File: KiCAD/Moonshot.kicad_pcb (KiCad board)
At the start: 2 copper layers, 33.7 x 40 mm, 16 parts, among them J1 USB-AF-DIP-154-HW-S_P1, J2 USB-AF-DIP-154-HW-S_P2, J3 DE9_Plug, J6 no impl., SW1 SW_Push, U1 CH559L, U2 74LS257, U3 74LS257

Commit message: v3 pcb
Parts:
- added J4: HY2.0-4P, toyoshim:CONN-TH_4P-P2.00_HX20020-4A_2, F.Cu at (40.4, 48.6)
- moved J6 18.2 mm to (22.9, 49.5)
- moved U2 17.0 mm to (46.4, 40.1), turned to 90 degrees
- moved C5 12.5 mm to (43.6, 35.9), turned to 180 degrees
- moved C6 8.78 mm to (25.1, 35.9), turned to 180 degrees
- moved U1 7.01 mm to (36.2, 40.0), turned to -90 degrees
- moved C2 6.79 mm to (41.8, 39.6), turned to 90 degrees
- moved C1 4.58 mm to (41.8, 41.5), turned to -90 degrees
- moved U3 3.24 mm to (27.9, 40.1), turned to 90 degrees
- moved C4 2.67 mm to (34.3, 51.4)
- moved C3 2.21 mm to (18.4, 51.4)
- moved R1 0.90 mm to (47.6, 49.5)
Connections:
- U1 pad 38: unconnected-(U1-P0_2-Pad38) -> /SDA
- U1 pad 39: unconnected-(U1-P0_1-Pad39) -> /SCL
- U1 pad 43: unconnected-(U1-P1_0-Pad43) -> /SDA
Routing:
- net /SCL: track 0.00 -> 70.5 mm, vias 0 -> 2
- net /B5: track 61.9 -> 15.4 mm
- net /B2: track 47.9 -> 6.81 mm, vias 2 -> 0
- net /JOY_B2: track 15.7 -> 56.6 mm, vias 1 -> 0
- net /START: track 51.9 -> 13.5 mm, vias 2 -> 0
- net /B6: track 54.1 -> 15.8 mm, vias 2 -> 0
- net VCC: track 84.6 -> 120.9 mm, vias 1 -> 2
- net /BTN: track 52.2 -> 17.9 mm, vias 2 -> 0
- net /B4: track 34.1 -> 8.01 mm
- net /B1: track 28.7 -> 52.1 mm
- net /SDA: track 0.00 -> 21.8 mm
- net /UP: track 13.4 -> 35.1 mm
- net GND: track 153.1 -> 170.6 mm, vias 1 -> 2
- net /TXD: track 4.97 -> 22.3 mm, vias 0 -> 2
- net /JOY_U: track 17.7 -> 34.7 mm
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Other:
- board text added: "2023.11.25 Rev.3 Designed By Mellow PCB MP17-MOONSHOT"
- board text added: "GND VCC SDA SCL"
- board text added: "I"
- board text added: "□"
- board text removed: "2023.10.22 Rev.2 Designed By Mellow PCB MP17-MOONSHOT"

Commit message: Moonshot rev.4 board
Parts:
- moved C5 0.76 mm to (42.8, 35.9)
- moved U2 0.76 mm to (45.6, 40.1)
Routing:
- net GND: track 170.6 -> 98.1 mm, vias 2 -> 8
- net /SCL: track 70.5 -> 10.8 mm, vias 2 -> 1
- net /JOY_B2: track 56.6 -> 13.6 mm, vias 0 -> 1
- net /B1: track 52.1 -> 18.8 mm
- net /JOY_R: track 10.5 -> 35.8 mm, vias 0 -> 1
- net VCC: track 120.9 -> 96.2 mm, vias 2 -> 3
- net /JOY_COM: track 85.4 -> 66.7 mm, vias 3 -> 2
- net /TXD: track 22.3 -> 36.6 mm, vias 2 -> 1
- net /JOY_D: track 20.7 -> 10.7 mm
- net /OE: track 35.1 -> 44.7 mm, vias 2 -> 3
- net /JOY_U: track 34.7 -> 25.2 mm
- net /SDA: track 21.8 -> 13.2 mm
- net /B6: track 15.8 -> 24.4 mm
- net /H2_D-: track 17.7 -> 9.74 mm
- net /UP: track 35.1 -> 43.0 mm, vias 2 -> 0
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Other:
- copper layers 2 -> 4
- board text added: "2023.12.29 Rev.4 Designed By Mellow PCB MP14-MOONSHOT"
- board text added: "MP14"
- board text removed: "2023.11.25 Rev.3 Designed By Mellow PCB MP17-MOONSHOT"
- board text removed: "MP17"

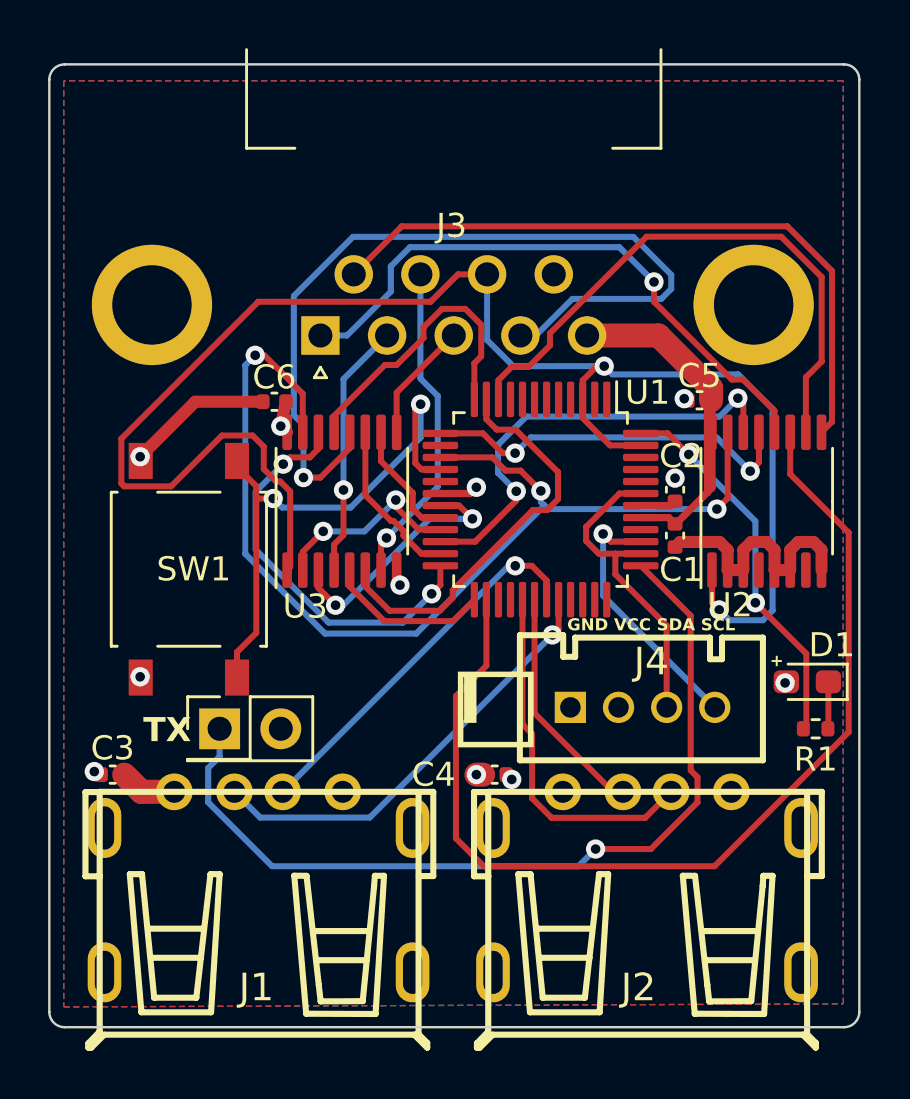
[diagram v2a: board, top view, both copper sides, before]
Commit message: fix the product # from 17 to 14
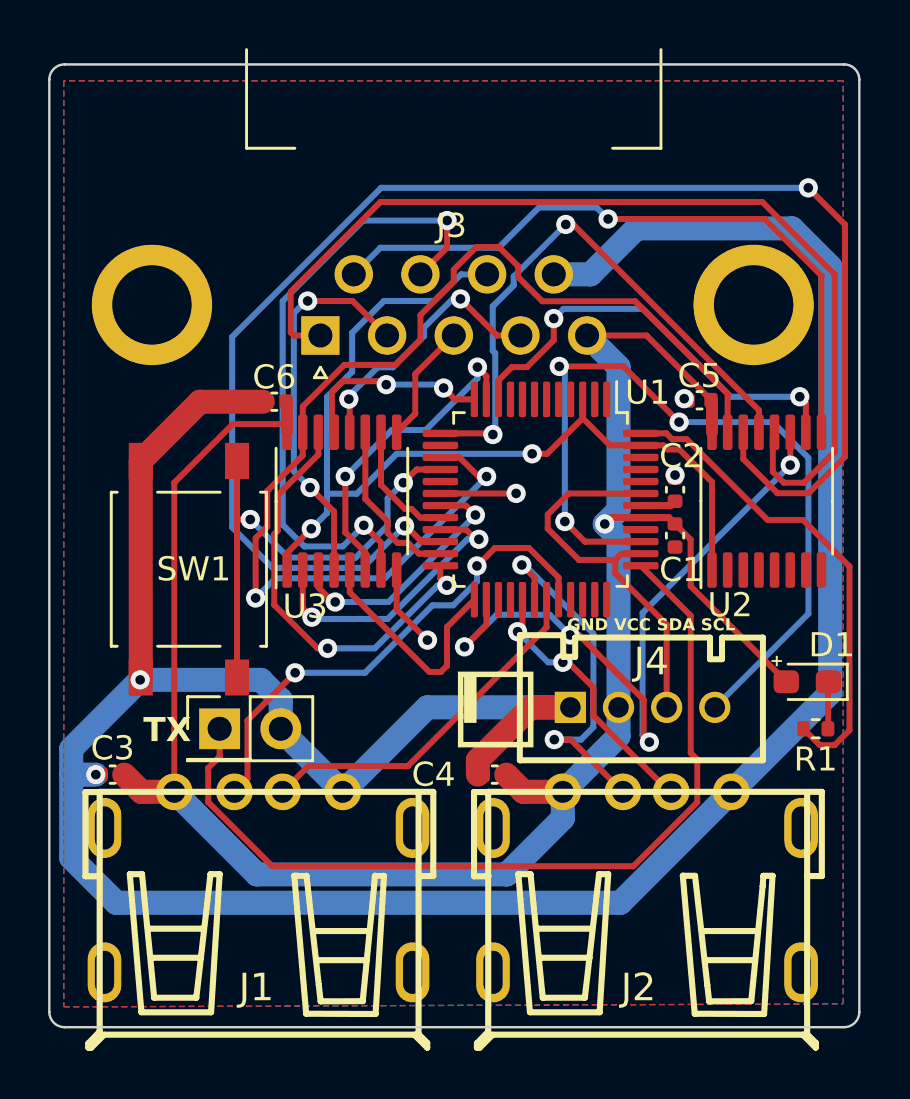
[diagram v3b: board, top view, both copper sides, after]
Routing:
- net /B1: track 18.8 -> 63.1 mm
- net GND: track 98.1 -> 125.2 mm, vias 8 -> 6
- net /JOY_COM: track 66.7 -> 40.4 mm
- net /JOY_R: track 35.8 -> 11.2 mm, vias 1 -> 2
- net /SCL: track 10.8 -> 33.9 mm, vias 1 -> 3
- net /JOY_U: track 25.2 -> 40.7 mm, vias 1 -> 0
- net /UP: track 43.0 -> 29.2 mm, vias 0 -> 4
- net /JOY_B2: track 13.6 -> 26.5 mm, vias 1 -> 2
- net VCC: track 96.2 -> 84.7 mm, vias 3 -> 1
- net /B3: track 15.8 -> 24.4 mm
- net /B6: track 24.4 -> 18.2 mm, vias 0 -> 2
- net /H2_D-: track 9.74 -> 15.3 mm, vias 0 -> 2
- net /JOY_D: track 10.7 -> 16.0 mm, vias 1 -> 2
- net Net-(U1-P1_5): track 15.8 -> 20.2 mm, vias 2 -> 0
- net /B4: track 12.4 -> 8.13 mm, vias 0 -> 2
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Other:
- copper layers 4 -> 2
- board text added: "2023.12.29 Rev.5 Designed By Mellow PCB MP14-MOONSHOT"
- board text removed: "2023.12.29 Rev.4 Designed By Mellow PCB MP14-MOONSHOT"

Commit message: Rev.5 board
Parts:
- added R2: 1k, Resistor_SMD:R_0402_1005Metric, F.Cu at (47.4, 35.8)
- added R3: 1k, Resistor_SMD:R_0402_1005Metric, F.Cu at (29.6, 44.8)
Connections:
- U2 pad 9: /JOY_B1 -> Net-(U2-Zd)
- U3 pad 7: /JOY_B2 -> Net-(U3-Zb)
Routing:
- net /JOY_B2: track 26.5 -> 32.0 mm
- net GND: track 125.2 -> 129.3 mm, vias 6 -> 7
- net /DOWN: track 9.66 -> 13.6 mm
- net /JOY_U: track 40.7 -> 44.1 mm
- net /B1: track 63.1 -> 65.8 mm
- net /B6: track 18.2 -> 20.2 mm
- net /SCL: track 33.9 -> 32.4 mm
- net /JOY_B1: track 28.3 -> 26.9 mm
- net Net-(U3-Zb): track 0.00 -> 1.40 mm
- net Net-(U2-Zd): track 0.00 -> 1.15 mm
- net /OE: track 48.4 -> 49.0 mm
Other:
- board text added: "2024.01.26 Rev.6 Designed By Mellow PCB MP14-MOONSHOT"
- board text removed: "2023.12.29 Rev.5 Designed By Mellow PCB MP14-MOONSHOT"

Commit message: PCB Rev.7
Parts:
- R2, R3: value 1k -> 100
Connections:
- U1 pad 10: /B6 -> /B3
- U1 pad 11: /B5 -> /START
- U1 pad 12: /B4 -> /SELECT
- U1 pad 13: /B3 -> /B6
- U1 pad 19: /START -> /B5
- U1 pad 20: /SELECT -> /B4
- U1 pad 21: /B2 -> /DOWN
- U1 pad 22: /B1 -> /UP
- U1 pad 23: /RIGHT -> /LEFT
- U1 pad 24: /LEFT -> /RIGHT
- U1 pad 25: /DOWN -> /B2
- U1 pad 26: /UP -> /B1
- U2 pad 10: /B6 -> /B3
- U2 pad 11: /UP -> /B1
- U2 pad 13: /B3 -> /B6
- U2 pad 14: /B1 -> /UP
- U3 pad 10: /SELECT -> /B4
- U3 pad 11: /RIGHT -> /LEFT
- U3 pad 13: /B4 -> /SELECT
- U3 pad 14: /LEFT -> /RIGHT
- U3 pad 2: /B2 -> /DOWN
- U3 pad 3: /START -> /B5
- U3 pad 5: /DOWN -> /B2
- U3 pad 6: /B5 -> /START
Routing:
- net /UP: track 29.3 -> 65.8 mm, vias 4 -> 2
- net /B1: track 65.8 -> 29.3 mm, vias 2 -> 4
- net /RIGHT: track 7.12 -> 17.9 mm, vias 0 -> 2
- net /LEFT: track 17.9 -> 7.12 mm, vias 2 -> 0
- net /B6: track 20.2 -> 24.4 mm
- net /B3: track 24.4 -> 20.2 mm
- net /SELECT: track 5.22 -> 8.21 mm, vias 0 -> 2
- net /B4: track 8.21 -> 5.22 mm, vias 2 -> 0
- net /START: track 10.6 -> 13.4 mm
- net /B5: track 13.4 -> 10.6 mm
- net /DOWN: track 13.6 -> 12.2 mm, vias 0 -> 2
- net /B2: track 12.2 -> 13.6 mm, vias 2 -> 0
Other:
- board text added: "2024.03.28 Rev.7 Designed By Mellow PCB MP14-MOONSHOT"
- board text removed: "2024.01.26 Rev.6 Designed By Mellow PCB MP14-MOONSHOT"
